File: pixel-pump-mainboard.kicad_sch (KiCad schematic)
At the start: 121 parts, among them J1 JST NC Valve, J10 BM10B-SRSS-TB(LF)(SN), J11 UART/SWD DNP, J12 TYPE-C-31-M-12, J2 JST NO Valve, J3 6P4C, J4 JST 3 Way Valve, J5 Jack-DC 12V, J6 Power Sw, J7 I2C, J8 SPI, J9 BM04B-SRSS-TBT(LF)(SN), Q1 BSS138, Q2 BSS138, Q3 BSS138, Q4 STN4NF20L, Q5 BSS138, SW1 BOOTSEL, U1 LD1117S33TR, U2 TPS62112RSAR, U3 W25Q128JVS, U4 RP2040, Y1 ABMM2-12.000MHZ-E2-T

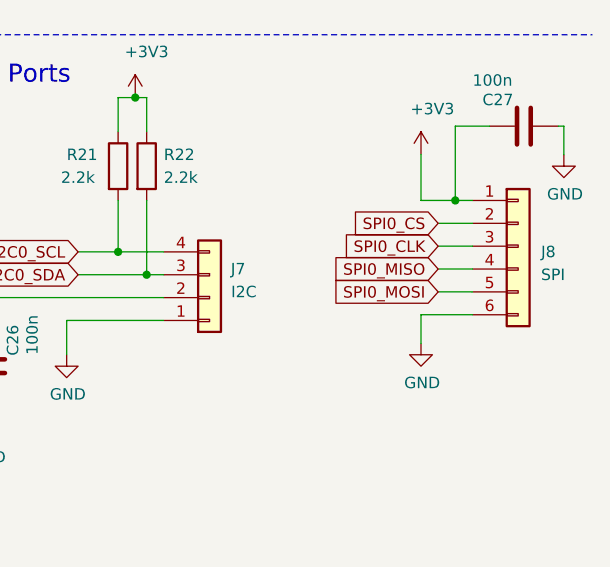
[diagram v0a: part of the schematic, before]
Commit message: Rename ports to EXP1 and EXP2 and reduce mousebite stiffness
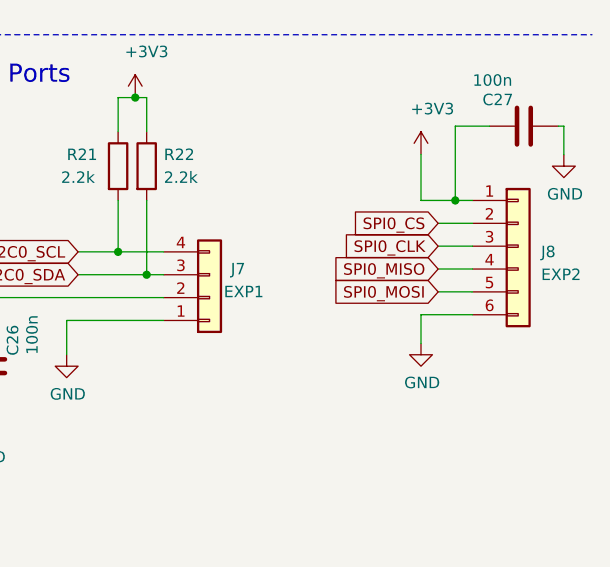
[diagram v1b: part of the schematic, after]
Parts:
- J7: value I2C -> EXP1
- J8: value SPI -> EXP2
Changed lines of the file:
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@@
     (in_bom yes) (on_board yes)
     (property "Reference" "J7" (id 0) (at 367.03 230.505 0))
-    (property "Value" "I2C" (id 1) (at 367.665 233.045 0))
+    (property "Value" "EXP1" (id 1) (at 367.665 233.045 0))
     (property "Footprint" "Connector_JST:JST_SH_BM04B-SRSS-TB_1x04-1MP_P1.00mm_Vertical" (id 2) (at 363.855 233.68 0)
       (effects (font (size 1.27 1.27)) hide)
@@
       (effects (font (size 1.27 1.27)) (justify left))
     )
-    (property "Value" "SPI" (id 1) (at 400.685 231.14 0)
+    (property "Value" "EXP2" (id 1) (at 400.685 231.14 0)
       (effects (font (size 1.27 1.27)) (justify left))
     )
@@
     )
     (path "/63c15b5e-c12a-4523-afda-c3d21e50ba5b"
-      (reference "J7") (unit 1) (value "I2C") (footprint "Connector_JST:JST_SH_BM04B-SRSS-TB_1x04-1MP_P1.00mm_Vertical")
+      (reference "J7") (unit 1) (value "EXP1") (footprint "Connector_JST:JST_SH_BM04B-SRSS-TB_1x04-1MP_P1.00mm_Vertical")
     )
     (path "/ccde1372-9ab3-47ad-9572-4de6238d460d"
-      (reference "J8") (unit 1) (value "SPI") (footprint "Connector_JST:JST_SH_BM06B-SRSS-TB_1x06-1MP_P1.00mm_Vertical")
+      (reference "J8") (unit 1) (value "EXP2") (footprint "Connector_JST:JST_SH_BM06B-SRSS-TB_1x06-1MP_P1.00mm_Vertical")
     )
     (path "/e5c2696e-219e-4607-9e22-8a199dce175a"
